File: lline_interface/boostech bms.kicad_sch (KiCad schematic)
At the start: 11 parts, among them J2 Conn_02x05_Odd_Even, Q1 DMN2050L, Q2 Q_NMOS_SGD, Q3 DMN2050L, U3 PIC12F675-xSN, U4 SG-107F, U5 NSL-32, U6 NSL-32

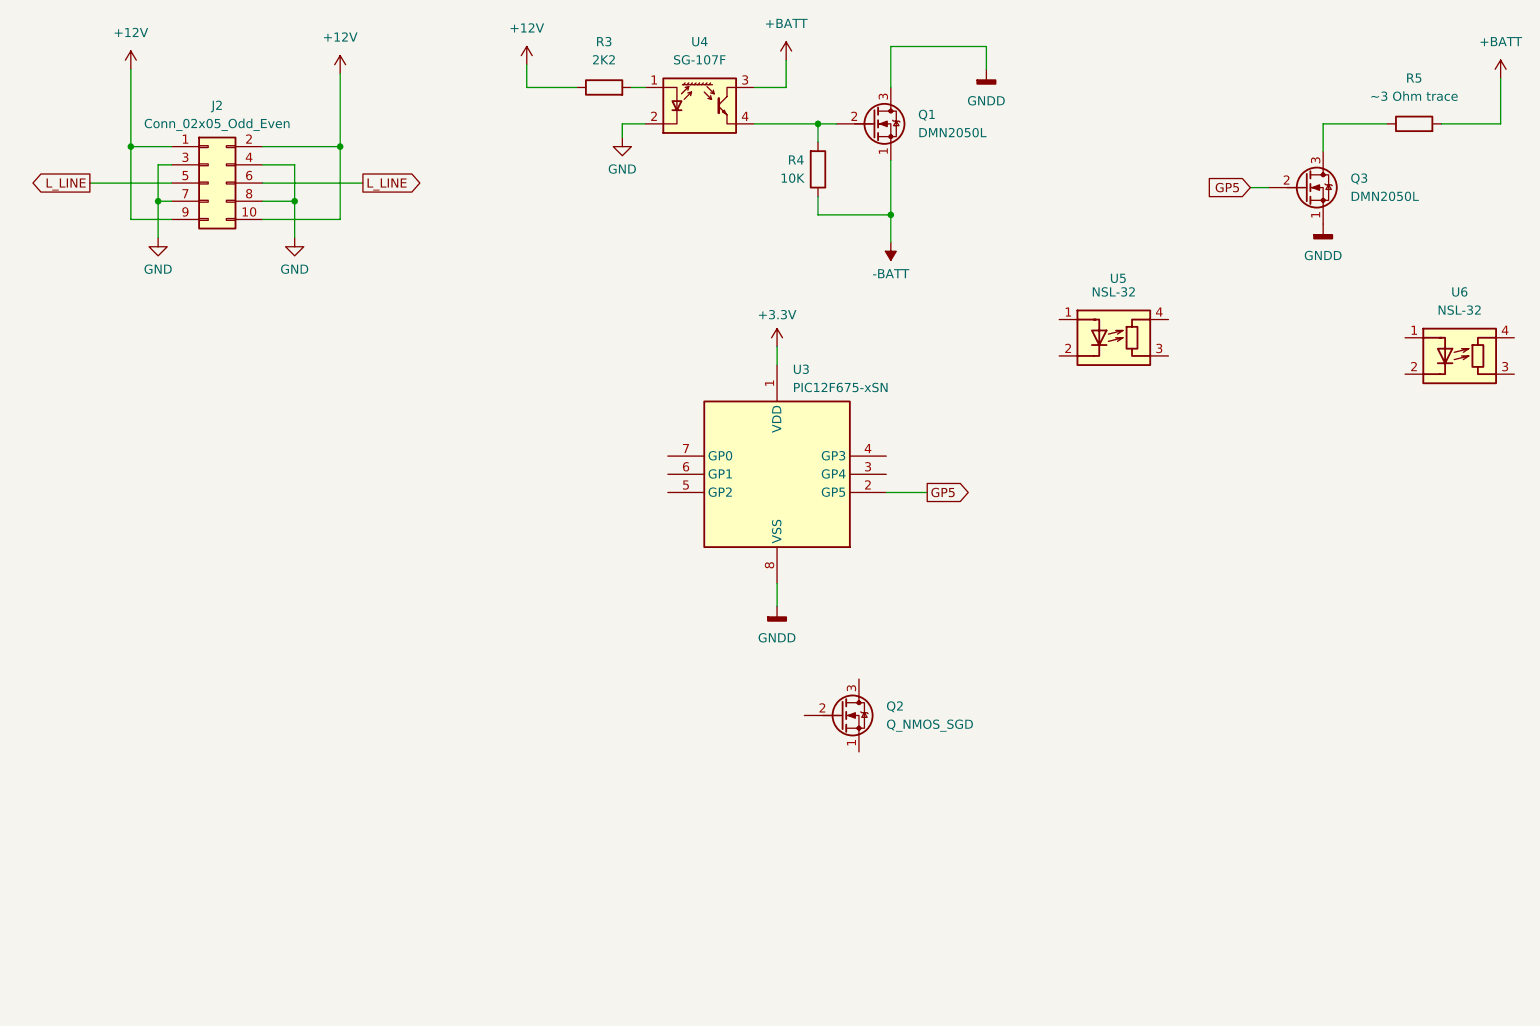
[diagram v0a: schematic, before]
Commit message: Start adding STM32 based master
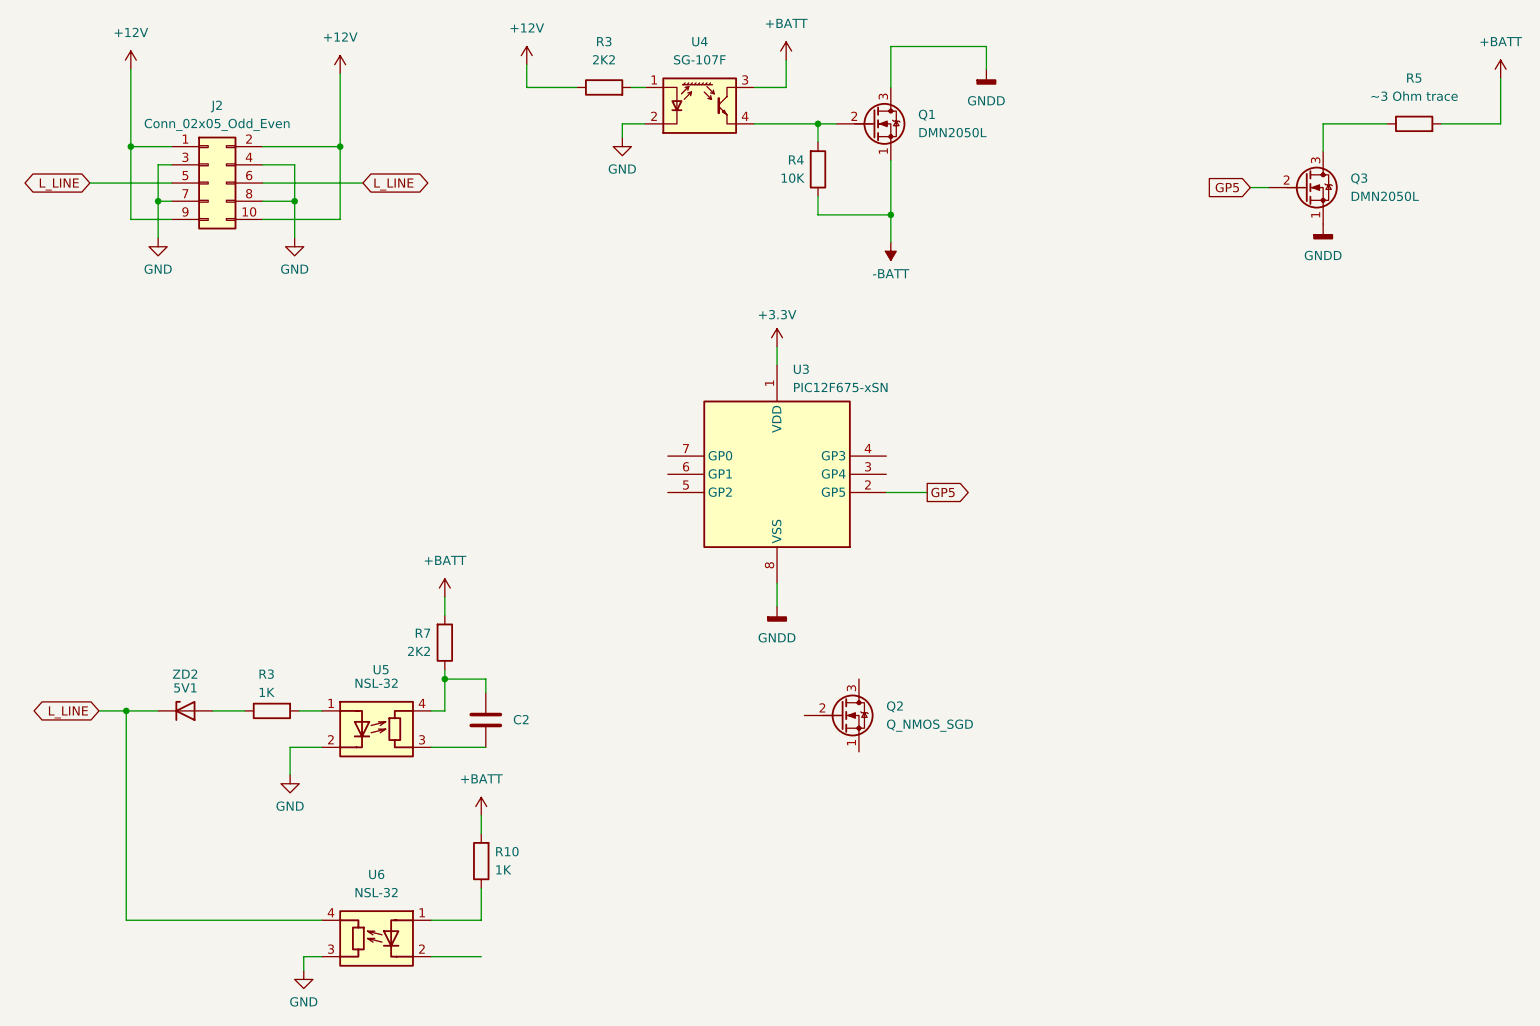
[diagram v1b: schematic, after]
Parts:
- added C2: C, symbol Device:C
- added R10, R3: 1K, symbol Device:R
- added R7: 2K2, symbol Device:R
- added ZD2: 5V1, symbol Device:D_Zener
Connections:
- net +BATT: now also R10.2, R7.2
- net GND: now also U5.2 (K), U6.3 (R)
- net L_LINE: now also U6.4 (R), ZD2.1 (K)
- net at U5.1 (A): now also R3.2
- net at U5.3 (R): now also C2.2
- net at U5.4 (R): now also C2.1, R7.1
- net at U6.1 (A): now also R10.1
- new net: R3.1, ZD2.2 (A)
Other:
- moved on the sheet: U5, U6
